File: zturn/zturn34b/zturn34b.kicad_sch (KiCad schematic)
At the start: 27 parts, among them U1 74AXP4T245, U2 74AXP4T245, U3 74AXP4T245, U4 74AXP4T245, U5 74AXP4T245

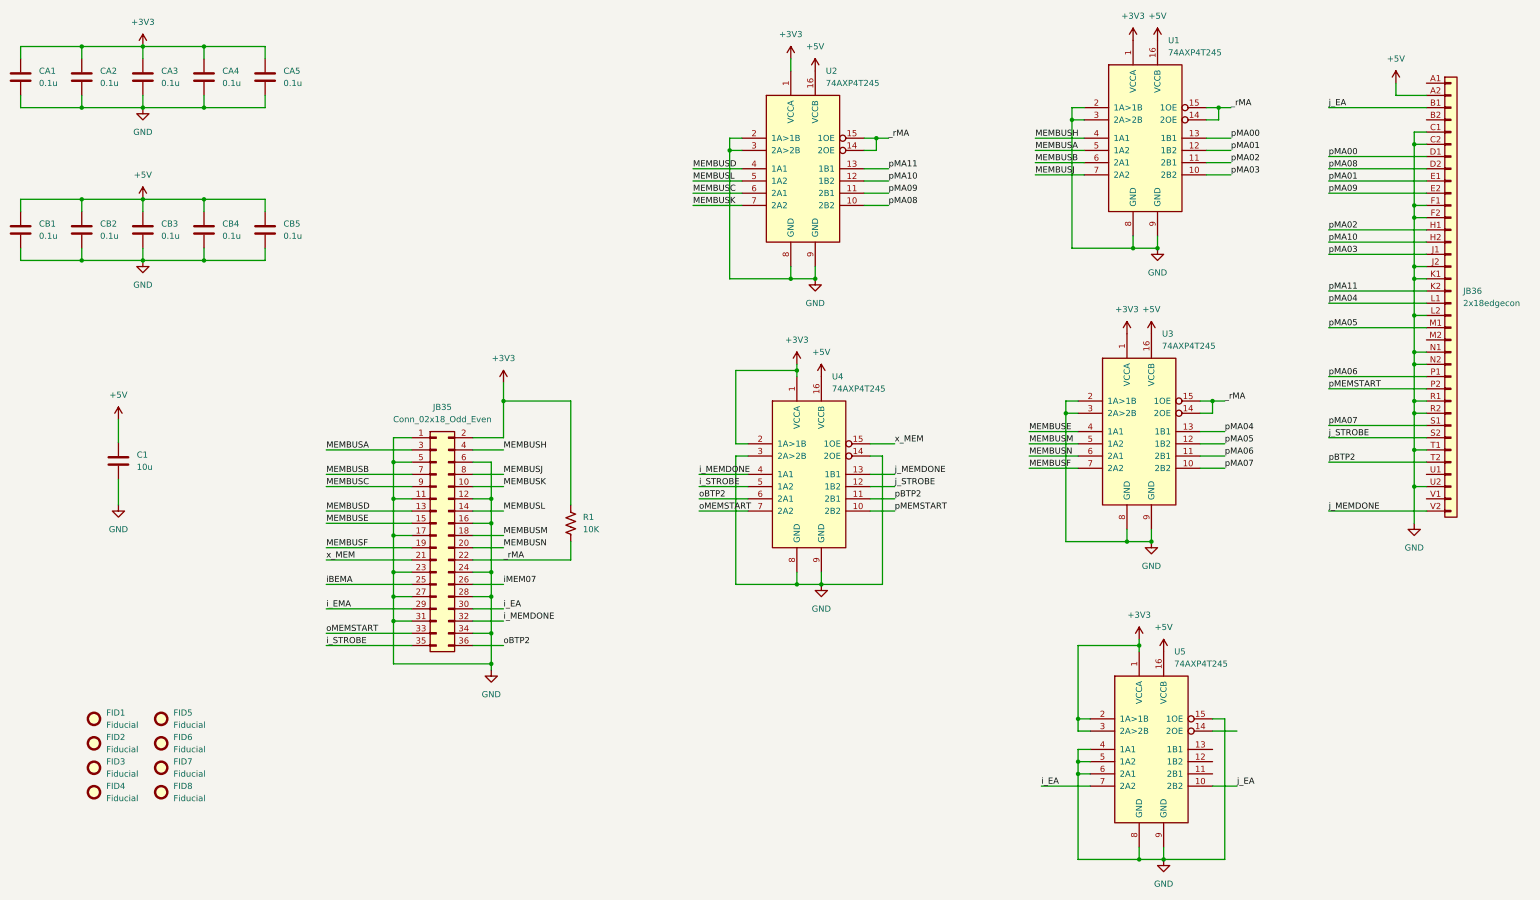
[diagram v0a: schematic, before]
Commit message: update net names on zturn pcbs to match active high/low signal type
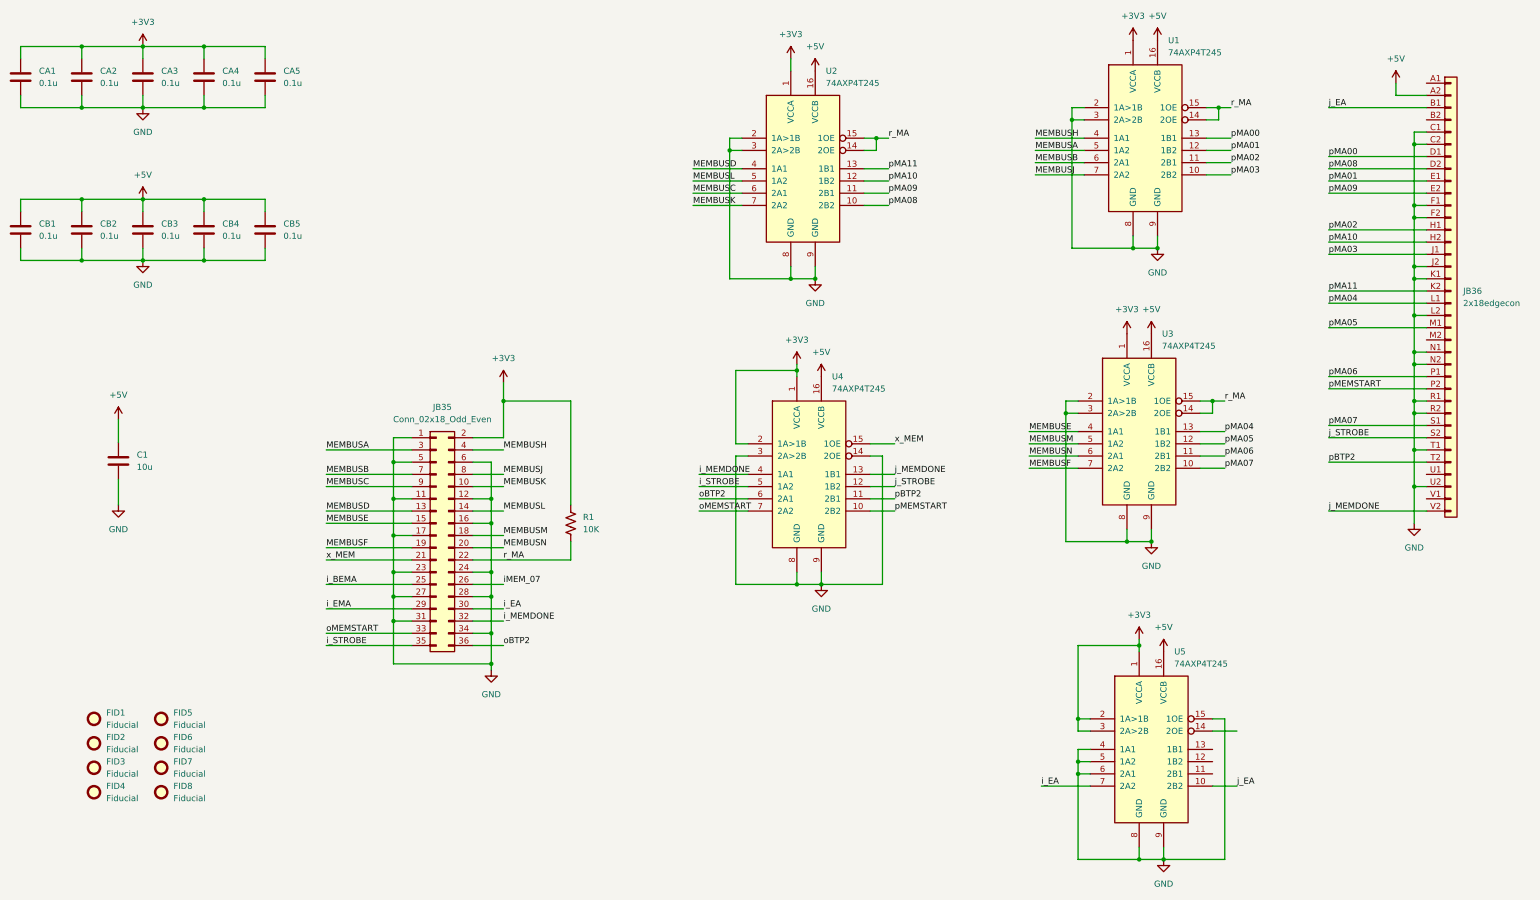
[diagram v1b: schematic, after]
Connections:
- net _rMA renamed r_MA
- net iBEMA renamed i_BEMA
- net iMEM07 renamed iMEM_07
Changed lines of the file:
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@@
     (effects (font (size 1.27 1.27)) (justify left bottom))
   )
-  (label "_rMA" (at 259.08 85.09 0) (fields_autoplaced)
+  (label "r_MA" (at 259.08 85.09 0) (fields_autoplaced)
     (effects (font (size 1.27 1.27)) (justify left bottom))
   )
@@
     (effects (font (size 1.27 1.27)) (justify left bottom))
   )
-  (label "_rMA" (at 189.23 30.48 0) (fields_autoplaced)
+  (label "r_MA" (at 189.23 30.48 0) (fields_autoplaced)
     (effects (font (size 1.27 1.27)) (justify left bottom))
   )
@@
     (effects (font (size 1.27 1.27)) (justify left bottom))
   )
-  (label "iMEM07" (at 109.22 123.19 0) (fields_autoplaced)
+  (label "iMEM_07" (at 109.22 123.19 0) (fields_autoplaced)
     (effects (font (size 1.27 1.27)) (justify left bottom))
   )
@@
     (effects (font (size 1.27 1.27)) (justify left bottom))
   )
-  (label "_rMA" (at 109.22 118.11 0) (fields_autoplaced)
+  (label "r_MA" (at 109.22 118.11 0) (fields_autoplaced)
     (effects (font (size 1.27 1.27)) (justify left bottom))
   )
-  (label "_rMA" (at 260.35 24.13 0) (fields_autoplaced)
+  (label "r_MA" (at 260.35 24.13 0) (fields_autoplaced)
     (effects (font (size 1.27 1.27)) (justify left bottom))
   )
@@
     (effects (font (size 1.27 1.27)) (justify left bottom))
   )
-  (label "iBEMA" (at 72.39 123.19 0) (fields_autoplaced)
+  (label "i_BEMA" (at 72.39 123.19 0) (fields_autoplaced)
     (effects (font (size 1.27 1.27)) (justify left bottom))
   )

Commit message: update software and further updates to firmware/pcbs
...for invertering transistors

./z8lsimtest works
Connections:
- net iMEM_07 renamed i_MEM_07
- net i_BEMA renamed iBEMA
- net i_EMA renamed iEMA
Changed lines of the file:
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@@
     (effects (font (size 1.27 1.27)) (justify left bottom))
   )
-  (label "iMEM_07" (at 109.22 123.19 0) (fields_autoplaced)
+  (label "i_MEM_07" (at 109.22 123.19 0) (fields_autoplaced)
     (effects (font (size 1.27 1.27)) (justify left bottom))
   )
@@
     (effects (font (size 1.27 1.27)) (justify left bottom))
   )
-  (label "i_EMA" (at 72.39 128.27 0) (fields_autoplaced)
+  (label "iEMA" (at 72.39 128.27 0) (fields_autoplaced)
     (effects (font (size 1.27 1.27)) (justify left bottom))
   )
@@
     (effects (font (size 1.27 1.27)) (justify left bottom))
   )
-  (label "i_BEMA" (at 72.39 123.19 0) (fields_autoplaced)
+  (label "iBEMA" (at 72.39 123.19 0) (fields_autoplaced)
     (effects (font (size 1.27 1.27)) (justify left bottom))
   )

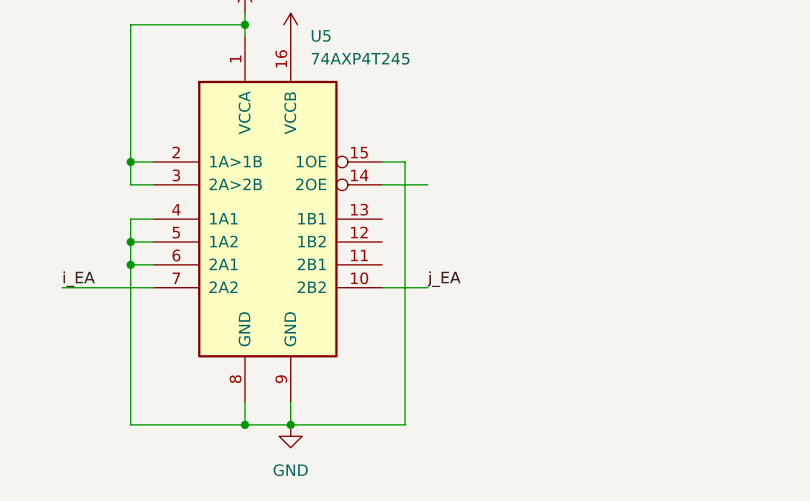
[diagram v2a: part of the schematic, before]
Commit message: fixed polarity of bus signals for the open-drain transistors
    PDP         Zynq
    MEM         _MEM
    MEM_P       _MEM_P
    _DMAADDR    DMAADDR
    _DMADATA    DMADATA
    _INPUTBUS   INPUTBUS

Also fixed MEMINCR polarity and fixed missing ground connection on circuit board.
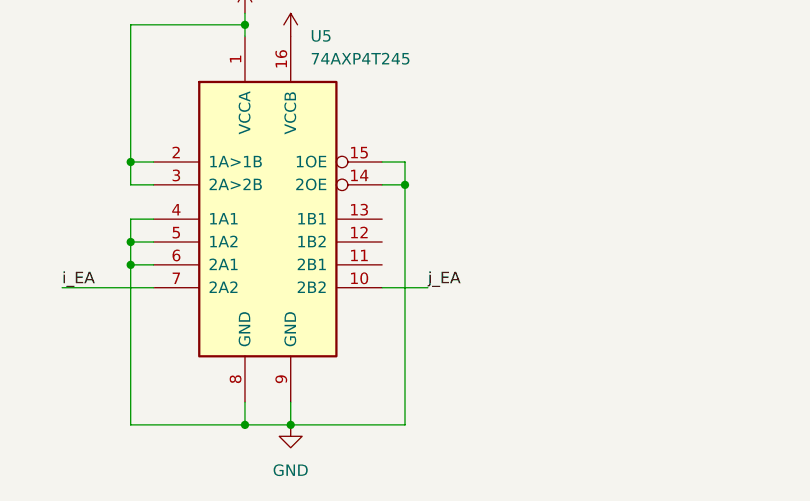
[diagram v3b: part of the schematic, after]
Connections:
- net GND: now also U5.14 (2OE)
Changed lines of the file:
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@@
   (junction (at 34.29 43.18) (diameter 0) (color 0 0 0 0)
   )
+  (junction (at 259.08 153.67) (diameter 0) (color 0 0 0 0)
+  )
   (junction (at 298.45 74.93) (diameter 0) (color 0 0 0 0)
   )
@@
     (stroke (width 0) (type default))
   )
-  (wire (pts (xy 256.54 153.67) (xy 261.62 153.67))
-    (stroke (width 0) (type default))
-  )
   (wire (pts (xy 168.91 13.97) (xy 168.91 16.51))
     (stroke (width 0) (type default))
@@
     (stroke (width 0) (type default))
   )
-  (wire (pts (xy 259.08 151.13) (xy 259.08 180.34))
+  (wire (pts (xy 259.08 151.13) (xy 259.08 153.67))
     (stroke (width 0) (type default))
   )
@@
     (stroke (width 0) (type default))
   )
+  (wire (pts (xy 259.08 153.67) (xy 259.08 180.34))
+    (stroke (width 0) (type default))
+  )
   (wire (pts (xy 34.29 21.59) (xy 34.29 24.13))
     (stroke (width 0) (type default))
@@
     (stroke (width 0) (type default))
   )
+  (wire (pts (xy 256.54 153.67) (xy 259.08 153.67))
+    (stroke (width 0) (type default))
+  )
